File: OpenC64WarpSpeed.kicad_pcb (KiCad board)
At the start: 2 copper layers, 58.4 x 61.7 mm, 18 parts, among them P1 C64-Exp-Port, SW1 SW_C64_C128, SW2 SW_RESET, SW3 SW_ROM, U1 74LS109, U2 27512

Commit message: Add license claim
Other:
- board text added: "Licensed under CERN OHL v.1.2"
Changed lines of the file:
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@@
   (general
     (thickness 1.6)
-    (drawings 22)
+    (drawings 23)
     (tracks 376)
     (zones 0)
@@
     (0 F.Cu signal)
     (31 B.Cu signal)
-    (36 B.SilkS user hide)
+    (36 B.SilkS user)
     (37 F.SilkS user)
     (38 B.Mask user)
@@
     )
   )
+  (gr_text "Licensed under CERN OHL v.1.2" (at 88.899999 117.729) (layer B.SilkS)
+    (effects (font (size 1 1) (thickness 0.15)) (justify mirror))
+  )
   (gr_text ROM2 (at 72.368 83.185) (layer F.SilkS)
     (effects (font (size 1 1) (thickness 0.15)))
@@
     (effects (font (size 1 1) (thickness 0.15)) (justify mirror))
   )
-  (gr_text github.com/SukkoPera/OpenC64WarpSpeed (at 89.0905 115.443) (layer B.SilkS)
+  (gr_text github.com/SukkoPera/OpenC64WarpSpeed (at 88.899999 113.157) (layer B.SilkS)
     (effects (font (size 1 1) (thickness 0.15)) (justify mirror))
   )

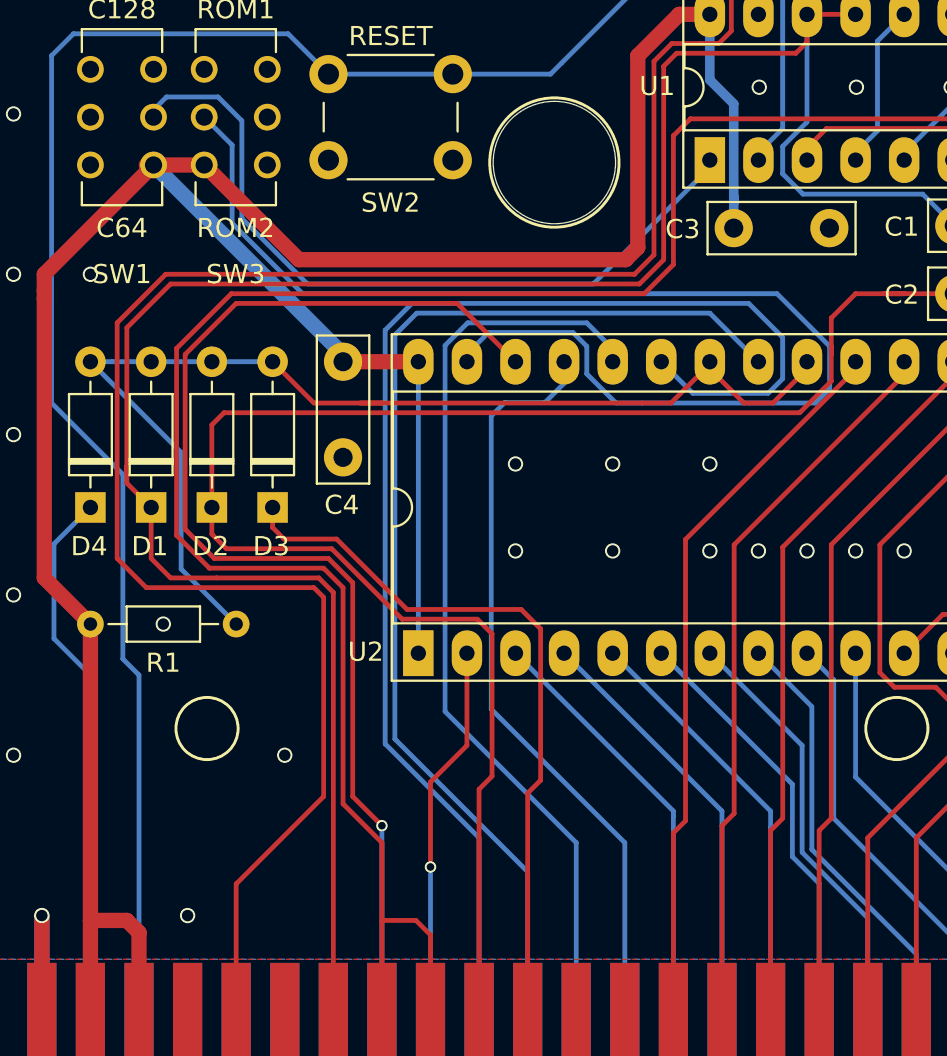
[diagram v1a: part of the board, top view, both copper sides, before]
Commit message: Add OSHW logo
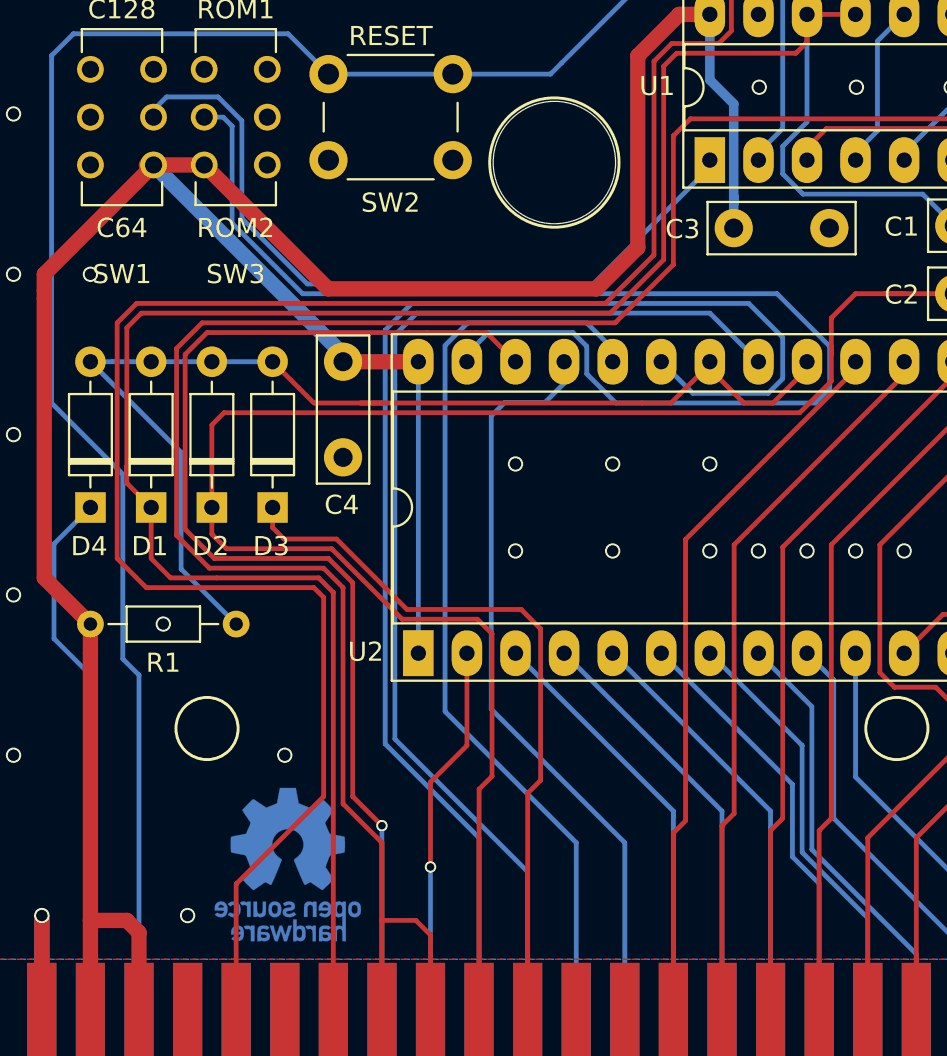
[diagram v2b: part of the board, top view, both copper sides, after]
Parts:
- added V0: OSHW_LOGO, Symbol:OSHW-Logo_7.5x8mm_Copper, B.Cu at (75.1, 116.5)
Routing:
- net +5V: track 145.6 -> 146.9 mm
- net /a13: track 63.2 -> 61.9 mm
- net Net-(SW3-Pad2): track 64.8 -> 65.4 mm

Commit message: Fix capacitor value: 470nF -> 47pF - Thanks @svenpetersen1965
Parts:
- C1, C2: value 470n -> 47p
